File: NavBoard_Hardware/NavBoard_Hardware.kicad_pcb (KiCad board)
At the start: 2 copper layers, 61 x 100.1 mm, 43 parts, among them J1 Conn_Coaxial, U3 OKI, U4 OKI, U5 FGPMMOPA6H

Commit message: BOM and other files for review
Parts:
- C7: footprint Capacitor_SMD:C_0603_1608Metric_Pad1.05x0.95mm_HandSolder -> Capacitor_THT:CP_Radial_D6.3mm_P2.50mm
- moved C7 7.28 mm to (170.2, 77.6), turned to 0 degrees
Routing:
- net Net-(D11-Pad2): track 1.65 -> 2.18 mm
- net /EXAnt: track 48.0 -> 48.6 mm

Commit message: just in case push
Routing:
- net +3V3: track 34.8 -> 28.2 mm, vias 2 -> 1
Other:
- board text added: "FIX"
- board text added: "RX"
- board text added: "TX"
- board text removed: "RX(SRC)"
- board text removed: "TX(SRC)"
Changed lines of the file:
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@@
   (general
     (thickness 1.6)
-    (drawings 69)
-    (tracks 306)
+    (drawings 72)
+    (tracks 298)
     (zones 0)
     (modules 43)
@@
       (outputformat 1)
       (mirror false)
-      (drillshape 1)
+      (drillshape 0)
       (scaleselection 1)
-      (outputdirectory ""))
+      (outputdirectory "../Documentation/Gerbs/"))
   )
   (net 0 "")
@@
     (tags "LED handsolder")
     (attr smd)
-    (fp_text reference D1 (at 0 -1.524) (layer F.SilkS)
+    (fp_text reference D1 (at 2.794 0.889) (layer F.SilkS)
       (effects (font (size 1 1) (thickness 0.15)))
     )
@@
     )
   )
+  (gr_text "FIX\n" (at 144.526 82.042) (layer F.SilkS)
+    (effects (font (size 1.5 1.5) (thickness 0.3)))
+  )
+  (gr_circle (center 151.13 72.644) (end 152.4 72.898) (layer F.SilkS) (width 0.2))
+  (gr_line (start 147.066 71.12) (end 149.352 71.12) (layer F.SilkS) (width 0.2))
   (gr_arc (start 117.2972 54.478921) (end 117.399059 52.3748) (angle -83.65369847) (layer Edge.Cuts) (width 0.15))
   (gr_arc (start 174.1805 54.356) (end 176.2125 54.356) (angle -93.93289733) (layer Edge.Cuts) (width 0.15))
@@
     (effects (font (size 1.5 1.5) (thickness 0.3)))
   )
-  (gr_text +3V3 (at 158.75 60.706 90) (layer B.SilkS)
+  (gr_text +3V3 (at 158.242 61.214 90) (layer B.SilkS)
     (effects (font (size 1.5 1.5) (thickness 0.3)) (justify mirror))
   )
-  (gr_text "SCL\n" (at 155.956 61.468 90) (layer B.SilkS)
+  (gr_text "SCL\n" (at 155.702 61.976 90) (layer B.SilkS)
     (effects (font (size 1.5 1.5) (thickness 0.3)) (justify mirror))
   )
-  (gr_text SDA (at 153.162 61.468 90) (layer B.SilkS)
+  (gr_text SDA (at 153.162 61.976 90) (layer B.SilkS)
     (effects (font (size 1.5 1.5) (thickness 0.3)) (justify mirror))
   )
-  (gr_text "DRDYM\n" (at 150.876 59.944 90) (layer B.SilkS)
+  (gr_text "DRDYM\n" (at 150.622 60.452 90) (layer B.SilkS)
     (effects (font (size 1.5 1.5) (thickness 0.3)) (justify mirror))
   )
-  (gr_text "INTM\n" (at 148.336 61.214 90) (layer B.SilkS)
+  (gr_text "INTM\n" (at 148.082 61.722 90) (layer B.SilkS)
     (effects (font (size 1.5 1.5) (thickness 0.3)) (justify mirror))
   )
-  (gr_text INT1AG (at 145.542 59.944 90) (layer B.SilkS)
+  (gr_text INT1AG (at 145.796 60.452 90) (layer B.SilkS)
     (effects (font (size 1.5 1.5) (thickness 0.3)) (justify mirror))
   )
-  (gr_text INT2AG (at 143.002 59.944 90) (layer B.SilkS)
+  (gr_text INT2AG (at 143.256 60.452 90) (layer B.SilkS)
     (effects (font (size 1.5 1.5) (thickness 0.3)) (justify mirror))
   )
-  (gr_text "GND\n" (at 140.462 60.96 90) (layer B.SilkS)
+  (gr_text "GND\n" (at 140.716 61.976 90) (layer B.SilkS)
     (effects (font (size 1.5 1.5) (thickness 0.3)) (justify mirror))
   )
@@
     (effects (font (size 1.5 1.5) (thickness 0.3)) (justify mirror))
   )
-  (gr_text +5V (at 164.592 60.706 90) (layer B.SilkS)
+  (gr_text +5V (at 164.592 61.722 90) (layer B.SilkS)
     (effects (font (size 1.5 1.5) (thickness 0.3)) (justify mirror))
   )
-  (gr_text SCL (at 167.386 60.706 90) (layer B.SilkS)
+  (gr_text SCL (at 167.386 61.976 90) (layer B.SilkS)
     (effects (font (size 1.5 1.5) (thickness 0.3)) (justify mirror))
   )
-  (gr_text SDA (at 170.18 60.706 90) (layer B.SilkS)
+  (gr_text SDA (at 170.18 61.976 90) (layer B.SilkS)
     (effects (font (size 1.5 1.5) (thickness 0.3)) (justify mirror))
   )
-  (gr_text "GND\n" (at 172.72 60.706 90) (layer B.SilkS)
+  (gr_text "GND\n" (at 172.72 61.722 90) (layer B.SilkS)
     (effects (font (size 1.5 1.5) (thickness 0.3)) (justify mirror))
   )
@@
   )
   (gr_line (start 143.8965 109.474) (end 143.8965 102.235) (layer F.SilkS) (width 0.2))
-  (gr_text "RX(SRC)" (at 146.9445 107.696) (layer F.SilkS)
+  (gr_text RX (at 147.32 107.696) (layer F.SilkS)
     (effects (font (size 0.992 0.992) (thickness 0.248)))
   )
-  (gr_text "TX(SRC)\n" (at 146.9445 104.394) (layer F.SilkS)
+  (gr_text "TX\n" (at 147.32 104.394) (layer F.SilkS)
     (effects (font (size 0.992 0.992) (thickness 0.248)))
   )
@@
   (via (at 149.1035 111.633) (size 0.8) (drill 0.4) (layers F.Cu B.Cu) (net 7))
   (segment (start 150.7685 111.633) (end 149.1035 111.633) (width 0.381) (layer F.Cu) (net 7))
-  (segment (start 117.2606 124.994402) (end 117.270798 124.994402) (width 0.508) (layer B.Cu) (net 7))
-  (segment (start 116.500601 125.754401) (end 117.2606 124.994402) (width 0.508) (layer B.Cu) (net 7))
-  (segment (start 117.270798 124.994402) (end 117.7544 124.5108) (width 0.508) (layer B.Cu) (net 7))
-  (segment (start 117.7544 124.5108) (end 117.7544 121.6152) (width 0.508) (layer B.Cu) (net 7))
-  (segment (start 117.7544 121.6152) (end 117.7798 121.5898) (width 0.508) (layer B.Cu) (net 7))
-  (segment (start 117.7798 121.5898) (end 117.7798 121.2596) (width 0.508) (layer B.Cu) (net 7))
-  (via (at 117.729 115.316) (size 0.8) (drill 0.4) (layers F.Cu B.Cu) (net 7))
-  (segment (start 117.7798 121.2596) (end 117.7798 115.3668) (width 0.508) (layer B.Cu) (net 7))
-  (segment (start 117.7798 115.3668) (end 117.729 115.316) (width 0.508) (layer B.Cu) (net 7))
   (segment (start 157.936951 96.595951) (end 157.861 96.52) (width 0.381) (layer F.Cu) (net 7))
   (segment (start 158.369 97.028) (end 157.861 96.52) (width 0.25) (layer F.Cu) (net 7))
@@
   (segment (start 157.08762 67.76401) (end 144.45299 67.76401) (width 0.381) (layer F.Cu) (net 7))
   (segment (start 158.242 66.60963) (end 157.08762 67.76401) (width 0.381) (layer F.Cu) (net 7))
+  (segment (start 117.651102 124.6039) (end 117.651102 121.870898) (width 0.381) (layer B.Cu) (net 7))
+  (segment (start 116.500601 125.754401) (end 117.651102 124.6039) (width 0.381) (layer B.Cu) (net 7))
   (segment (start 143.665 80.25) (end 143.651 80.264) (width 0.381) (layer F.Cu) (net 8))
   (segment (start 143.665 78.232) (end 143.665 80.25) (width 0.381) (layer F.Cu) (net 8))
@@
   (segment (start 172.530101 87.806262) (end 172.72 87.616363) (width 0.381) (layer F.Cu) (net 37))
   (segment (start 172.530101 91.299363) (end 172.530101 87.806262) (width 0.381) (layer F.Cu) (net 37))
-  (segment (start 172.530101 103.567899) (end 170.18 105.918) (width 0.381) (layer F.Cu) (net 37))
-  (segment (start 172.530101 91.299363) (end 172.530101 103.567899) (width 0.381) (layer F.Cu) (net 37))
-  (segment (start 170.18 105.918) (end 158.369 105.918) (width 0.381) (layer F.Cu) (net 37))
-  (segment (start 158.369 105.918) (end 157.861 106.426) (width 0.381) (layer F.Cu) (net 37))
-  (segment (start 157.861 106.426) (end 157.861 112.141) (width 0.381) (layer F.Cu) (net 37))
-  (via (at 157.607 116.332) (size 0.8) (drill 0.4) (layers F.Cu B.Cu) (net 37))
-  (segment (start 157.861 112.141) (end 157.861 116.078) (width 0.381) (layer F.Cu) (net 37))
-  (segment (start 157.861 116.078) (end 157.607 116.332) (width 0.381) (layer F.Cu) (net 37))
-  (via (at 152.527 116.459) (size 0.8) (drill 0.4) (layers F.Cu B.Cu) (net 37))
-  (segment (start 157.607 116.332) (end 152.654 116.332) (width 0.381) (layer B.Cu) (net 37))
-  (segment (start 152.654 116.332) (end 152.527 116.459) (width 0.381) (layer B.Cu) (net 37))
-  (segment (start 150.885315 115.383) (end 150.7825 115.383) (width 0.381) (layer F.Cu) (net 37))
-  (segment (start 151.961315 116.459) (end 150.885315 115.383) (width 0.381) (layer F.Cu) (net 37))
-  (segment (start 152.527 116.459) (end 151.961315 116.459) (width 0.381) (layer F.Cu) (net 37))
   (segment (start 166.867388 71.363388) (end 167.673606 71.363388) (width 0.381) (layer F.Cu) (net 37))
   (segment (start 165.1 65.532) (end 165.1 69.596) (width 0.381) (layer F.Cu) (net 37))
@@
   (segment (start 172.72 77.597) (end 172.72 72.263) (width 0.381) (layer F.Cu) (net 37))
   (segment (start 172.72 72.263) (end 171.820388 71.363388) (width 0.381) (layer F.Cu) (net 37))
+  (segment (start 151.961315 116.459) (end 150.885315 115.383) (width 0.381) (layer F.Cu) (net 37))
+  (segment (start 150.885315 115.383) (end 150.7825 115.383) (width 0.381) (layer F.Cu) (net 37))
+  (segment (start 152.654 116.332) (end 152.527 116.459) (width 0.381) (layer B.Cu) (net 37))
+  (segment (start 152.527 116.459) (end 151.961315 116.459) (width 0.381) (layer F.Cu) (net 37))
+  (segment (start 172.530101 91.299363) (end 172.530101 103.567899) (width 0.381) (layer F.Cu) (net 37))
+  (segment (start 172.530101 103.567899) (end 170.18 105.918) (width 0.381) (layer F.Cu) (net 37))
+  (segment (start 170.18 105.918) (end 158.369 105.918) (width 0.381) (layer F.Cu) (net 37))
+  (via (at 152.527 116.459) (size 0.8) (drill 0.4) (layers F.Cu B.Cu) (net 37))
+  (segment (start 157.861 106.426) (end 158.369 105.918) (width 0.381) (layer B.Cu) (net 37))
+  (segment (start 157.353 116.459) (end 157.861 115.951) (width 0.381) (layer B.Cu) (net 37))
+  (segment (start 157.861 115.951) (end 157.861 106.426) (width 0.381) (layer B.Cu) (net 37))
+  (segment (start 152.527 116.459) (end 157.353 116.459) (width 0.381) (layer B.Cu) (net 37))
+  (via (at 158.369 105.918) (size 0.8) (drill 0.4) (layers F.Cu B.Cu) (net 37))
   (segment (start 133.520602 81.814402) (end 133.503402 81.814402) (width 0.381) (layer B.Cu) (net 38))
   (segment (start 134.280601 82.574401) (end 133.520602 81.814402) (width 0.381) (layer B.Cu) (net 38))

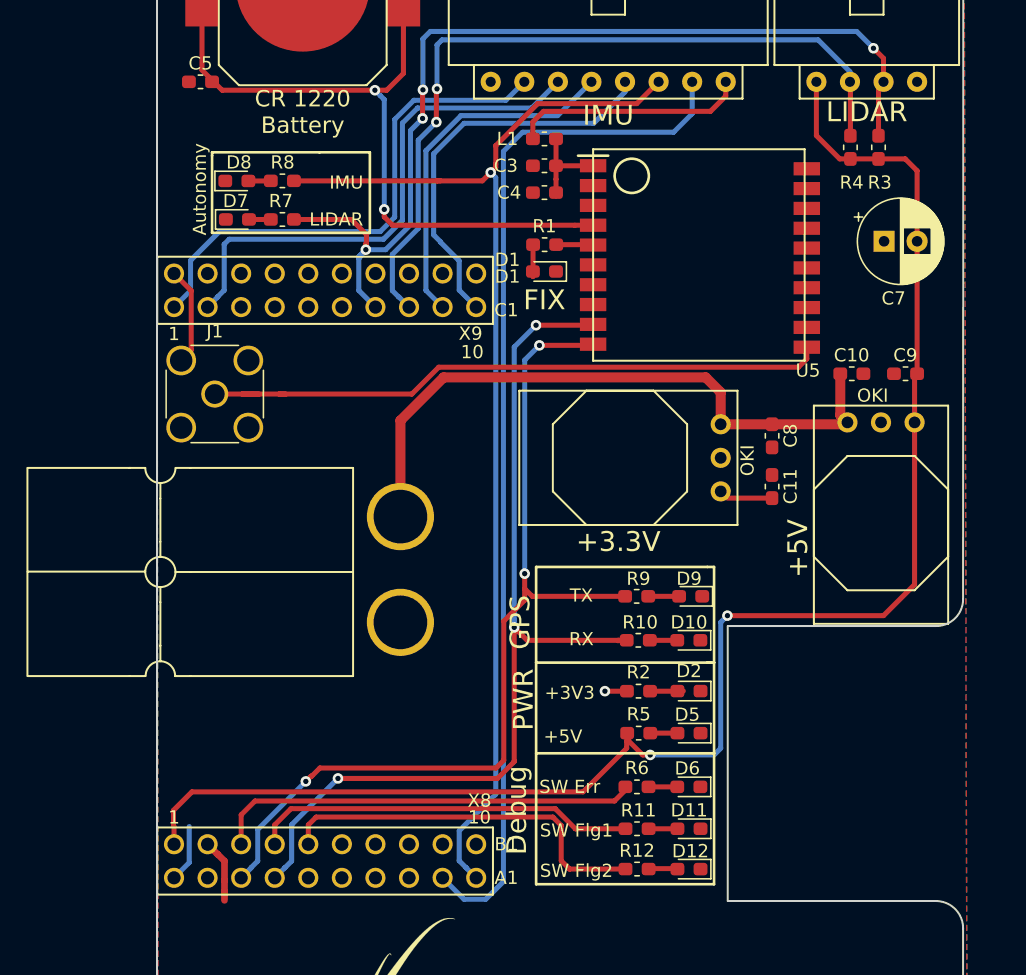
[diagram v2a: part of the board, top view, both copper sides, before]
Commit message: Updated to rev2 libraries
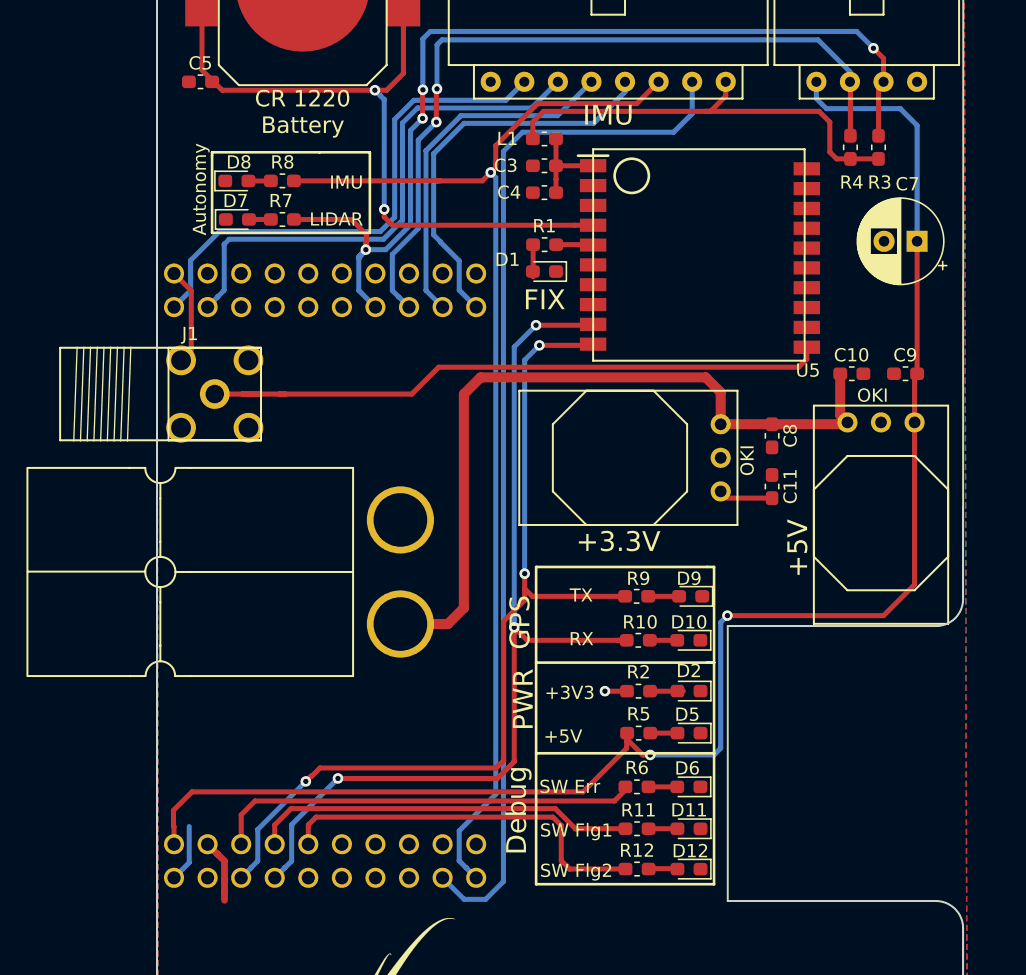
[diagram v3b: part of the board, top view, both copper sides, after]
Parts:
- Conn1: footprint MRDT_Connectors:Anderson_2_Horisontal_Side_by_Side -> MRDT_Connectors:Anderson_2_Horizontal_Side_by_Side
- J1: footprint Connector_Coaxial:SMA_Amphenol_132134-16_Vertical -> MRDT_Connectors:RP-SMA_Jack_Tru-Hole_Right-Angle
- U1: footprint MRDT_Shields:TM4C129E_Launchpad_X9 -> MRDT_Shields:TM4C129E_Launchpad_X9_THT_BOTTOM
- moved C7 2.50 mm to (172.7, 77.6), turned to 180 degrees
- turned J1 to 180 degrees
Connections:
- C7 pad 1: GND -> +5V
- C7 pad 2: +5V -> GND
- R3 pad 1: +5V -> +3V3
- R4 pad 2: +5V -> +3V3
- U1 pad PA6: Net-(U1-PadPA6) -> (no net)
- U1 pad PC6: Net-(U1-PadPC6) -> (no net)
- U1 pad PC7: Net-(U1-PadPC7) -> (no net)
- U1 pad PD0: Net-(U1-PadPD0) -> (no net)
- U1 pad PD1: Net-(U1-PadPD1) -> (no net)
- U1 pad PD3: Net-(U1-PadPD3) -> (no net)
- U1 pad PD7: Net-(U1-PadPD7) -> (no net)
- U1 pad PE3: Net-(U1-PadPE3) -> (no net)
- U1 pad PE4: Net-(U1-PadPE4) -> (no net)
- U1 pad PE5: Net-(U1-PadPE5) -> (no net)
- U1 pad PF3: Net-(U1-PadPF3) -> (no net)
- U1 pad PG0: Net-(U1-PadPG0) -> (no net)
- U1 pad PH2: Net-(U1-PadPH2) -> (no net)
- U1 pad PH3: Net-(U1-PadPH3) -> (no net)
- U1 pad PL4: Net-(U1-PadPL4) -> (no net)
- U1 pad PL5: Net-(U1-PadPL5) -> (no net)
- U1 pad PM3: Net-(U1-PadPM3) -> (no net)
- U1 pad PM4: Net-(U1-PadPM4) -> (no net)
- U1 pad PM5: Net-(U1-PadPM5) -> (no net)
- U1 pad PN2: Net-(U1-PadPN2) -> (no net)
- U1 pad PN3: Net-(U1-PadPN3) -> (no net)
- U1 pad PP2: Net-(U1-PadPP2) -> (no net)
- U1 pad Rese: Net-(U1-PadRese) -> (no net)
- U5 pad 13: Net-(U5-Pad13) -> (no net)
- U5 pad 14: Net-(U5-Pad14) -> (no net)
- U5 pad 15: Net-(U5-Pad15) -> (no net)
- U5 pad 16: Net-(U5-Pad16) -> (no net)
- U5 pad 17: Net-(U5-Pad17) -> (no net)
- U5 pad 18: Net-(U5-Pad18) -> (no net)
- U5 pad 2: Net-(U5-Pad2) -> (no net)
- U5 pad 20: Net-(U5-Pad20) -> (no net)
- U5 pad 6: Net-(U5-Pad6) -> (no net)
- U5 pad 7: Net-(U5-Pad7) -> (no net)
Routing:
- net +3V3: track 28.2 -> 44.1 mm
- net Net-(C10-Pad1): track 49.5 -> 58.1 mm
